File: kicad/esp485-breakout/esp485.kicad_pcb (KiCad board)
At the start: 2 copper layers, 25.4 x 26.2 mm, 15 parts, among them J1 Conn_01x08, J2 Conn_01x08, U1 MAX3485, U2 ESP-WROOM-02

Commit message: all done probably
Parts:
- removed FLASH, RESET: SW_Push, tact:generic tactile switch
- added FL: SW_Push, tact:tactile_switch_smd_4x3mm_2p, F.Cu at (136.0, 111.1)
- added RST: SW_Push, tact:tactile_switch_smd_4x3mm_2p, F.Cu at (145.9, 111.1)
- J1, J2: value Conn_01x08 -> Conn_01x07; footprint Pin_Headers:Pin_Header_Straight_1x08_Pitch2.54mm -> Pin_Headers:Pin_Header_Straight_1x07_Pitch2.54mm
- moved R10 15.5 mm to (147.3, 106.9)
- moved R4 12.8 mm to (134.4, 106.9)
- moved R5 12.6 mm to (136.7, 106.9), turned to 270 degrees
- moved R3 10.9 mm to (139.3, 97.5), turned to 90 degrees
- moved R2 8.52 mm to (137.0, 97.5), turned to 90 degrees
- moved R9 4.38 mm to (139.3, 102.6)
- moved R7 1.40 mm to (146.4, 99.7)
- moved R8 0.64 mm to (146.4, 97.5)
- moved U1 0.36 mm to (142.1, 106.8)
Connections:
- J1 pad 2: GND -> Net-(J1-Pad2)
- R10 pad 1: Net-(J2-Pad2) -> Net-(J1-Pad6)
- R5 pad 1: Net-(J2-Pad2) -> Net-(J1-Pad6)
- R7 pad 2: Net-(J2-Pad4) -> Net-(J2-Pad3)
- R9 pad 1: Net-(J1-Pad6) -> Net-(J1-Pad5)
- U1 pad 7: Net-(J2-Pad2) -> Net-(J1-Pad6)
- U2 pad 10: Net-(J2-Pad8) -> Net-(J2-Pad7)
- U2 pad 11: Net-(J2-Pad7) -> Net-(J2-Pad6)
- U2 pad 12: Net-(J2-Pad6) -> Net-(J2-Pad5)
- U2 pad 14: Net-(J2-Pad5) -> Net-(J2-Pad4)
- U2 pad 15: Net-(J2-Pad4) -> Net-(J2-Pad3)
- U2 pad 16: Net-(J2-Pad3) -> Net-(J2-Pad2)
- U2 pad 3: Net-(J1-Pad3) -> Net-(J1-Pad2)
- U2 pad 4: Net-(J1-Pad4) -> Net-(J1-Pad3)
- U2 pad 5: Net-(J1-Pad5) -> Net-(J1-Pad4)
- U2 pad 6: Net-(J1-Pad6) -> Net-(J1-Pad5)
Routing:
- net GND: track 97.7 -> 11.0 mm, vias 4 -> 3
- net Net-(J2-Pad2): track 39.5 -> 2.58 mm
- net Net-(R3-Pad1): track 15.7 -> 38.0 mm
- net Net-(J2-Pad4): track 17.2 -> 3.17 mm, vias 2 -> 0
- net Net-(J2-Pad3): track 3.54 -> 17.4 mm, vias 0 -> 2
- net Net-(J1-Pad6): track 10.5 -> 23.1 mm, vias 1 -> 3
- net Net-(R2-Pad1): track 13.8 -> 21.6 mm, vias 2 -> 3
- net +3V3: track 44.9 -> 37.1 mm
- net Net-(J2-Pad8): track 6.92 -> 0.00 mm
- net Net-(J2-Pad5): track 7.27 -> 2.98 mm, vias 1 -> 0
- net Net-(J1-Pad5): track 6.95 -> 10.6 mm
- net Net-(J1-Pad7): track 23.8 -> 21.2 mm, vias 0 -> 2
- net Net-(J1-Pad2): track 0.00 -> 2.55 mm
- net Net-(J2-Pad7): track 6.58 -> 4.38 mm
- net Net-(R8-Pad2): track 12.8 -> 14.4 mm
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- added copper zone on F.Cu, net GND
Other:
- board size 25.4 x 26.2 mm -> 25.4 x 22.9 mm
- board text added: "3V3"
- board text added: "A"
- board text added: "B"
- board text added: "GND"
- board text added: "IO12"
- board text added: "IO13"
- board text added: "IO14"
- board text added: "IO15"
- board text added: "IO4"
- board text added: "IO5"
- board text added: "RST"
- board text added: "RXD"
- board text added: "TOUT"
- board text added: "TXD"

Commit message: fix erratta
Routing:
- net Net-(J1-Pad6): track 23.1 -> 23.8 mm
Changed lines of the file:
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@@
     (thickness 1.6)
     (drawings 22)
-    (tracks 144)
+    (tracks 146)
     (zones 0)
     (modules 15)
@@
       (net 9 "Net-(J2-Pad3)"))
   )
-  (gr_text B (at 131.445 111.76) (layer B.SilkS)
-    (effects (font (size 1 1) (thickness 0.15)) (justify mirror))
-  )
-  (gr_text A (at 131.445 109.22) (layer B.SilkS)
+  (gr_text A (at 131.445 111.76) (layer B.SilkS)
+    (effects (font (size 1 1) (thickness 0.15)) (justify mirror))
+  )
+  (gr_text B (at 131.445 109.22) (layer B.SilkS)
     (effects (font (size 1 1) (thickness 0.15)) (justify mirror))
   )
@@
   (segment (start 137.16 109.22) (end 138.388 107.992) (width 0.25) (layer F.Cu) (net 2))
   (segment (start 129.54 109.22) (end 137.16 109.22) (width 0.25) (layer F.Cu) (net 2))
+  (segment (start 139.413 106.368998) (end 139.761001 106.716999) (width 0.25) (layer B.Cu) (net 2))
+  (segment (start 139.413 106.172) (end 139.413 106.368998) (width 0.25) (layer B.Cu) (net 2))
   (segment (start 131.526002 103.893) (end 131.953 103.893) (width 0.25) (layer F.Cu) (net 3))
   (segment (start 130.389999 105.029003) (end 131.526002 103.893) (width 0.25) (layer F.Cu) (net 3))

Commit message: done some optimization
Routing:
- net GND: track 11.0 -> 6.35 mm, vias 3 -> 2
- net Net-(J1-Pad7): track 21.2 -> 21.8 mm
- net Net-(J1-Pad6): track 23.8 -> 23.3 mm, vias 3 -> 4
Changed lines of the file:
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@@
     (thickness 1.6)
     (drawings 22)
-    (tracks 146)
+    (tracks 145)
     (zones 0)
     (modules 15)
@@
   (segment (start 130.91 111.76) (end 134.366 108.304) (width 0.25) (layer B.Cu) (net 1))
   (segment (start 129.54 111.76) (end 130.91 111.76) (width 0.25) (layer B.Cu) (net 1))
-  (via (at 139.413 107.442) (size 0.8) (drill 0.4) (layers F.Cu B.Cu) (net 1))
-  (segment (start 139.888 107.442) (end 140.65 106.68) (width 0.25) (layer F.Cu) (net 1))
-  (segment (start 139.413 107.442) (end 139.888 107.442) (width 0.25) (layer F.Cu) (net 1))
   (via (at 147.32 108.284) (size 0.8) (drill 0.4) (layers F.Cu B.Cu) (net 1))
-  (segment (start 140.65 106.68) (end 145.716 106.68) (width 0.25) (layer F.Cu) (net 1))
-  (segment (start 145.716 106.68) (end 147.32 108.284) (width 0.25) (layer F.Cu) (net 1))
+  (segment (start 147.32 107.284) (end 146.716 106.68) (width 0.25) (layer F.Cu) (net 1))
+  (segment (start 147.32 108.284) (end 147.32 107.284) (width 0.25) (layer F.Cu) (net 1))
+  (via (at 142.87808 106.812821) (size 0.8) (drill 0.4) (layers F.Cu B.Cu) (net 1))
+  (segment (start 146.716 106.68) (end 143.010901 106.68) (width 0.25) (layer F.Cu) (net 1))
+  (segment (start 143.010901 106.68) (end 142.87808 106.812821) (width 0.25) (layer F.Cu) (net 1))
+  (segment (start 142.248901 107.442) (end 139.413 107.442) (width 0.25) (layer B.Cu) (net 1))
+  (segment (start 142.87808 106.812821) (end 142.248901 107.442) (width 0.25) (layer B.Cu) (net 1))
   (segment (start 138.388 106.172) (end 139.413 106.172) (width 0.25) (layer B.Cu) (net 2))
   (segment (start 138.22 106.172) (end 138.388 106.172) (width 0.25) (layer B.Cu) (net 2))
   (segment (start 137.552 105.504) (end 138.22 106.172) (width 0.25) (layer B.Cu) (net 2))
   (segment (start 136.652 105.504) (end 137.552 105.504) (width 0.25) (layer B.Cu) (net 2))
-  (via (at 147.32 105.584) (size 0.8) (drill 0.4) (layers F.Cu B.Cu) (net 2))
   (via (at 139.413 106.172) (size 0.8) (drill 0.4) (layers F.Cu B.Cu) (net 2))
   (via (at 136.652 105.504) (size 0.8) (drill 0.4) (layers F.Cu B.Cu) (net 2))
-  (segment (start 146.558 106.172) (end 139.413 106.172) (width 0.25) (layer F.Cu) (net 2))
-  (segment (start 147.32 105.584) (end 147.146 105.584) (width 0.25) (layer F.Cu) (net 2))
-  (segment (start 147.146 105.584) (end 146.558 106.172) (width 0.25) (layer F.Cu) (net 2))
   (segment (start 138.938 106.172) (end 139.413 106.172) (width 0.25) (layer F.Cu) (net 2))
   (segment (start 138.388 106.722) (end 138.938 106.172) (width 0.25) (layer F.Cu) (net 2))
@@
   (segment (start 137.16 109.22) (end 138.388 107.992) (width 0.25) (layer F.Cu) (net 2))
   (segment (start 129.54 109.22) (end 137.16 109.22) (width 0.25) (layer F.Cu) (net 2))
-  (segment (start 139.413 106.368998) (end 139.761001 106.716999) (width 0.25) (layer B.Cu) (net 2))
   (segment (start 139.413 106.172) (end 139.413 106.368998) (width 0.25) (layer B.Cu) (net 2))
+  (via (at 147.32 105.584) (size 0.8) (drill 0.4) (layers F.Cu B.Cu) (net 2))
+  (via (at 142.987999 105.723002) (size 0.8) (drill 0.4) (layers F.Cu B.Cu) (net 2))
+  (segment (start 147.32 105.584) (end 143.127001 105.584) (width 0.25) (layer F.Cu) (net 2))
+  (segment (start 143.127001 105.584) (end 142.987999 105.723002) (width 0.25) (layer F.Cu) (net 2))
+  (segment (start 142.539001 106.172) (end 139.413 106.172) (width 0.25) (layer B.Cu) (net 2))
+  (segment (start 142.987999 105.723002) (end 142.539001 106.172) (width 0.25) (layer B.Cu) (net 2))
   (segment (start 131.526002 103.893) (end 131.953 103.893) (width 0.25) (layer F.Cu) (net 3))
   (segment (start 130.389999 105.029003) (end 131.526002 103.893) (width 0.25) (layer F.Cu) (net 3))
@@
   (segment (start 138.905 108.204) (end 139.413 108.712) (width 0.25) (layer B.Cu) (net 6))
   (segment (start 136.652 108.204) (end 138.905 108.204) (width 0.25) (layer B.Cu) (net 6))
-  (segment (start 137.922 111.125) (end 139.172 111.125) (width 0.25) (layer F.Cu) (net 6))
-  (segment (start 136.652 108.204) (end 136.652 109.855) (width 0.25) (layer B.Cu) (net 6))
-  (via (at 137.922 111.125) (size 0.8) (drill 0.4) (layers F.Cu B.Cu) (net 6))
-  (segment (start 136.652 109.855) (end 137.922 111.125) (width 0.25) (layer B.Cu) (net 6))
   (via (at 140.669 102.616) (size 0.8) (drill 0.4) (layers F.Cu B.Cu) (net 6))
   (via (at 136.652 108.204) (size 0.8) (drill 0.4) (layers F.Cu B.Cu) (net 6))

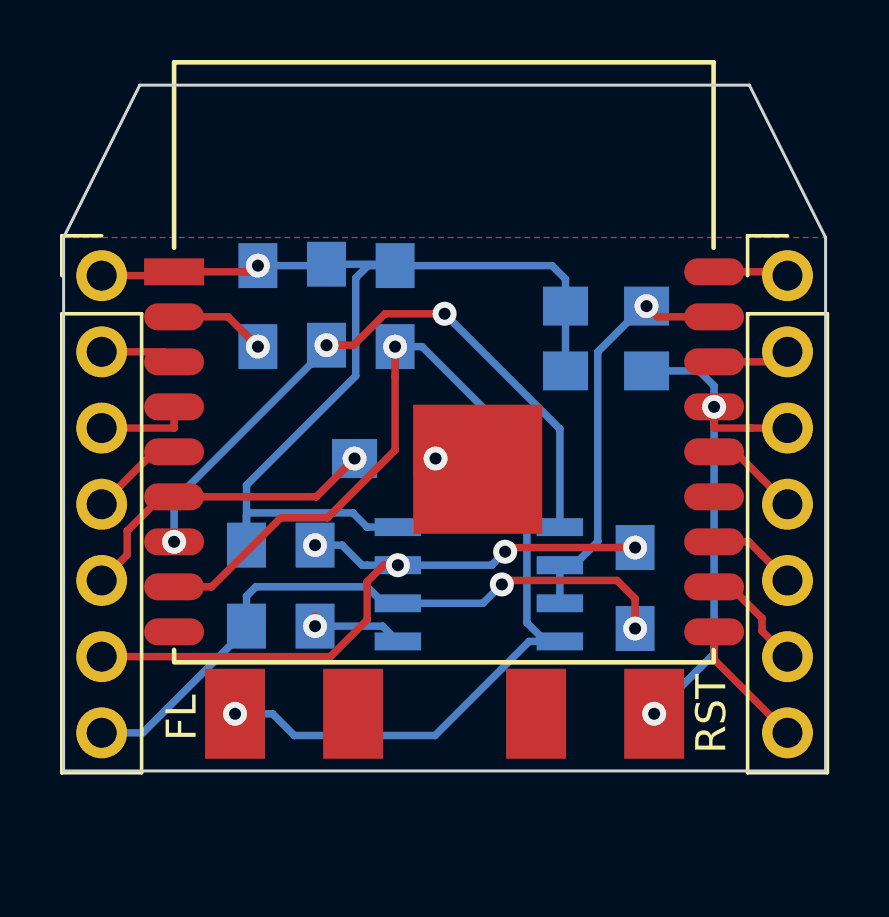
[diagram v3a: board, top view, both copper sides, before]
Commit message: gnd pattern optimized
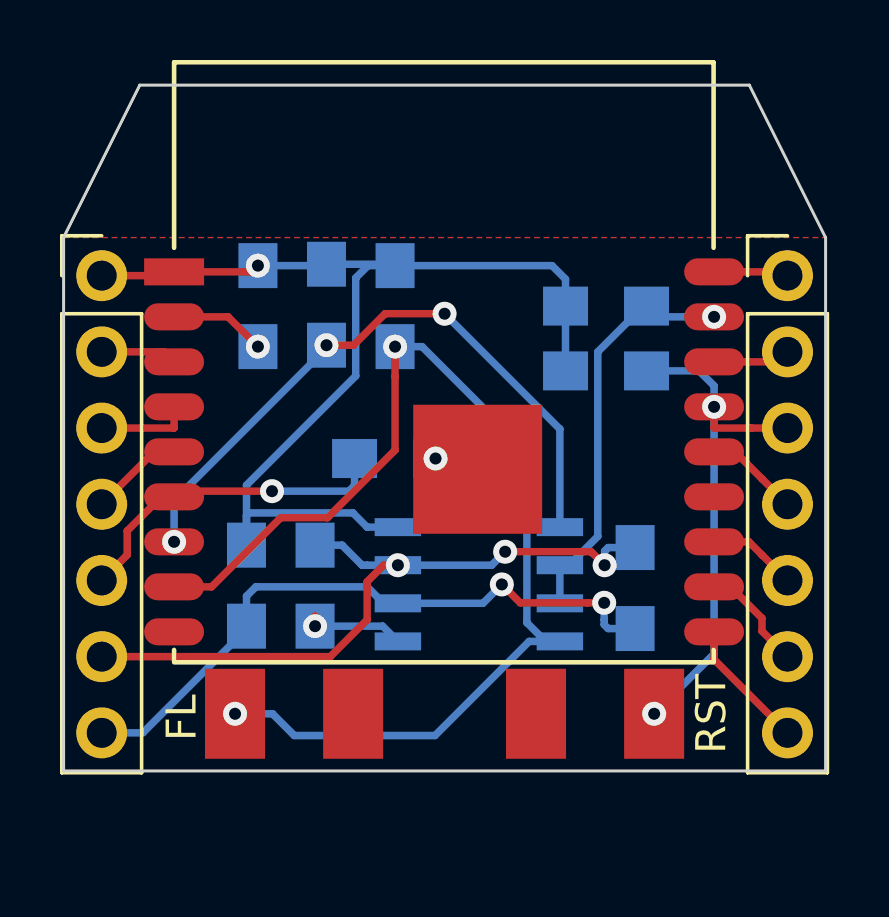
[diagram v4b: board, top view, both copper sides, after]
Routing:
- net Net-(J1-Pad6): track 23.3 -> 23.9 mm, vias 4 -> 3
- net Net-(J1-Pad5): track 10.6 -> 11.1 mm
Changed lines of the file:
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@@
     (thickness 1.6)
     (drawings 22)
-    (tracks 145)
+    (tracks 155)
     (zones 0)
     (modules 15)
@@
   (segment (start 130.91 111.76) (end 134.366 108.304) (width 0.25) (layer B.Cu) (net 1))
   (segment (start 129.54 111.76) (end 130.91 111.76) (width 0.25) (layer B.Cu) (net 1))
-  (via (at 147.32 108.284) (size 0.8) (drill 0.4) (layers F.Cu B.Cu) (net 1))
-  (segment (start 147.32 107.284) (end 146.716 106.68) (width 0.25) (layer F.Cu) (net 1))
-  (segment (start 147.32 108.284) (end 147.32 107.284) (width 0.25) (layer F.Cu) (net 1))
+  (segment (start 142.87808 106.812821) (end 142.248901 107.442) (width 0.25) (layer B.Cu) (net 1))
+  (segment (start 142.248901 107.442) (end 139.413 107.442) (width 0.25) (layer B.Cu) (net 1))
+  (segment (start 143.010901 106.68) (end 142.87808 106.812821) (width 0.25) (layer F.Cu) (net 1))
   (via (at 142.87808 106.812821) (size 0.8) (drill 0.4) (layers F.Cu B.Cu) (net 1))
-  (segment (start 146.716 106.68) (end 143.010901 106.68) (width 0.25) (layer F.Cu) (net 1))
-  (segment (start 143.010901 106.68) (end 142.87808 106.812821) (width 0.25) (layer F.Cu) (net 1))
-  (segment (start 142.248901 107.442) (end 139.413 107.442) (width 0.25) (layer B.Cu) (net 1))
-  (segment (start 142.87808 106.812821) (end 142.248901 107.442) (width 0.25) (layer B.Cu) (net 1))
+  (segment (start 147.32 108.284) (end 146.42 108.284) (width 0.25) (layer B.Cu) (net 1))
+  (segment (start 146.289432 107.99159) (end 146.289432 107.425905) (width 0.25) (layer B.Cu) (net 1))
+  (segment (start 143.491164 107.425905) (end 145.723747 107.425905) (width 0.25) (layer F.Cu) (net 1))
+  (segment (start 146.42 108.284) (end 146.289432 108.153432) (width 0.25) (layer B.Cu) (net 1))
+  (via (at 146.289432 107.425905) (size 0.8) (drill 0.4) (layers F.Cu B.Cu) (net 1))
+  (segment (start 145.723747 107.425905) (end 146.289432 107.425905) (width 0.25) (layer F.Cu) (net 1))
+  (segment (start 142.87808 106.812821) (end 143.491164 107.425905) (width 0.25) (layer F.Cu) (net 1))
+  (segment (start 146.289432 108.153432) (end 146.289432 107.99159) (width 0.25) (layer B.Cu) (net 1))
   (segment (start 138.388 106.172) (end 139.413 106.172) (width 0.25) (layer B.Cu) (net 2))
   (segment (start 138.22 106.172) (end 138.388 106.172) (width 0.25) (layer B.Cu) (net 2))
@@
   (segment (start 136.652 105.504) (end 137.552 105.504) (width 0.25) (layer B.Cu) (net 2))
   (via (at 139.413 106.172) (size 0.8) (drill 0.4) (layers F.Cu B.Cu) (net 2))
-  (via (at 136.652 105.504) (size 0.8) (drill 0.4) (layers F.Cu B.Cu) (net 2))
   (segment (start 138.938 106.172) (end 139.413 106.172) (width 0.25) (layer F.Cu) (net 2))
   (segment (start 138.388 106.722) (end 138.938 106.172) (width 0.25) (layer F.Cu) (net 2))
@@
   (segment (start 129.54 109.22) (end 137.16 109.22) (width 0.25) (layer F.Cu) (net 2))
   (segment (start 139.413 106.172) (end 139.413 106.368998) (width 0.25) (layer B.Cu) (net 2))
-  (via (at 147.32 105.584) (size 0.8) (drill 0.4) (layers F.Cu B.Cu) (net 2))
   (via (at 142.987999 105.723002) (size 0.8) (drill 0.4) (layers F.Cu B.Cu) (net 2))
-  (segment (start 147.32 105.584) (end 143.127001 105.584) (width 0.25) (layer F.Cu) (net 2))
-  (segment (start 143.127001 105.584) (end 142.987999 105.723002) (width 0.25) (layer F.Cu) (net 2))
   (segment (start 142.539001 106.172) (end 139.413 106.172) (width 0.25) (layer B.Cu) (net 2))
   (segment (start 142.987999 105.723002) (end 142.539001 106.172) (width 0.25) (layer B.Cu) (net 2))
+  (via (at 146.304 106.172002) (size 0.8) (drill 0.4) (layers F.Cu B.Cu) (net 2))
+  (segment (start 146.42 105.584) (end 146.304 105.7) (width 0.25) (layer B.Cu) (net 2))
+  (segment (start 146.304 105.7) (end 146.304 106.172002) (width 0.25) (layer B.Cu) (net 2))
+  (segment (start 147.32 105.584) (end 146.42 105.584) (width 0.25) (layer B.Cu) (net 2))
+  (segment (start 145.855 105.723002) (end 145.904001 105.772003) (width 0.25) (layer F.Cu) (net 2))
+  (segment (start 145.904001 105.772003) (end 146.304 106.172002) (width 0.25) (layer F.Cu) (net 2))
+  (segment (start 142.987999 105.723002) (end 145.855 105.723002) (width 0.25) (layer F.Cu) (net 2))
   (segment (start 131.526002 103.893) (end 131.953 103.893) (width 0.25) (layer F.Cu) (net 3))
   (segment (start 130.389999 105.029003) (end 131.526002 103.893) (width 0.25) (layer F.Cu) (net 3))
   (segment (start 130.389999 105.830001) (end 130.389999 105.029003) (width 0.25) (layer F.Cu) (net 3))
   (segment (start 129.54 106.68) (end 130.389999 105.830001) (width 0.25) (layer F.Cu) (net 3))
-  (via (at 137.969 102.616) (size 0.8) (drill 0.4) (layers F.Cu B.Cu) (net 3))
-  (segment (start 131.953 103.893) (end 136.692 103.893) (width 0.25) (layer F.Cu) (net 3))
-  (segment (start 136.692 103.893) (end 137.969 102.616) (width 0.25) (layer F.Cu) (net 3))
+  (via (at 135.216801 103.703999) (size 0.8) (drill 0.4) (layers F.Cu B.Cu) (net 3))
+  (segment (start 132.692001 103.703999) (end 135.216801 103.703999) (width 0.25) (layer F.Cu) (net 3))
+  (segment (start 131.953 103.893) (end 132.503 103.893) (width 0.25) (layer F.Cu) (net 3))
+  (segment (start 132.503 103.893) (end 132.692001 103.703999) (width 0.25) (layer F.Cu) (net 3))
+  (segment (start 137.969 103.516) (end 137.969 102.616) (width 0.25) (layer B.Cu) (net 3))
+  (segment (start 137.781001 103.703999) (end 137.969 103.516) (width 0.25) (layer B.Cu) (net 3))
+  (segment (start 135.216801 103.703999) (end 137.781001 103.703999) (width 0.25) (layer B.Cu) (net 3))
   (segment (start 131.287 102.393) (end 131.953 102.393) (width 0.25) (layer F.Cu) (net 4))
   (segment (start 129.54 104.14) (end 131.287 102.393) (width 0.25) (layer F.Cu) (net 4))
@@
   (segment (start 149.953 97.893) (end 149.403 97.893) (width 0.25) (layer F.Cu) (net 16))
   (segment (start 144.813 106.172) (end 144.813 107.442) (width 0.25) (layer B.Cu) (net 16))
-  (via (at 147.701 97.536) (size 0.8) (drill 0.4) (layers F.Cu B.Cu) (net 16))
-  (segment (start 149.953 97.893) (end 148.058 97.893) (width 0.25) (layer F.Cu) (net 16))
-  (segment (start 148.058 97.893) (end 147.701 97.536) (width 0.25) (layer F.Cu) (net 16))
-  (segment (start 145.288 106.172) (end 144.813 106.172) (width 0.25) (layer B.Cu) (net 16))
-  (segment (start 146.076001 105.383999) (end 145.288 106.172) (width 0.25) (layer B.Cu) (net 16))
+  (via (at 149.953 97.893) (size 0.8) (drill 0.4) (layers F.Cu B.Cu) (net 16))
+  (segment (start 148.058 97.893) (end 147.701 97.536) (width 0.25) (layer B.Cu) (net 16))
+  (segment (start 149.953 97.893) (end 148.058 97.893) (width 0.25) (layer B.Cu) (net 16))
+  (segment (start 146.076001 105.211009) (end 145.11501 106.172) (width 0.25) (layer B.Cu) (net 16))
   (segment (start 147.601 97.536) (end 146.076001 99.060999) (width 0.25) (layer B.Cu) (net 16))
-  (segment (start 146.076001 99.060999) (end 146.076001 105.383999) (width 0.25) (layer B.Cu) (net 16))
-  (segment (start 147.701 97.536) (end 147.601 97.536) (width 0.25) (layer B.Cu) (net 16))
+  (segment (start 145.11501 106.172) (end 144.813 106.172) (width 0.25) (layer B.Cu) (net 16))
+  (segment (start 146.076001 99.060999) (end 146.076001 105.211009) (width 0.25) (layer B.Cu) (net 16))
   (via (at 139.319 98.886) (size 0.8) (drill 0.4) (layers F.Cu B.Cu) (net 17))
   (segment (start 139.319 98.886) (end 140.219 98.886) (width 0.25) (layer B.Cu) (net 17))
